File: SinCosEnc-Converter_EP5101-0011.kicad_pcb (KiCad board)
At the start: 2 copper layers, 88 x 49.3 mm, 4 parts, among them U1 iC-NV, X1 Conn_02x06_Top_Bottom, X2 D-SUB-DR-15PCG-AB

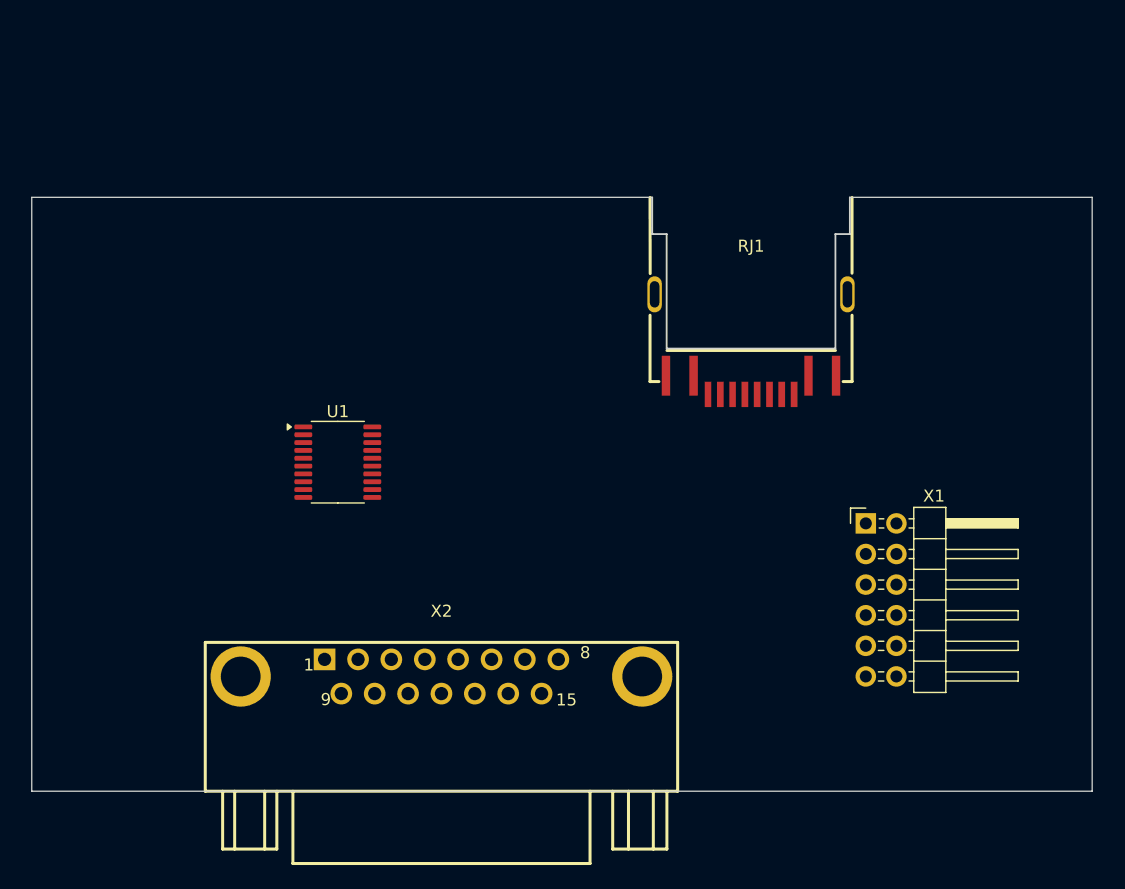
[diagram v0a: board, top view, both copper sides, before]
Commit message: schematic finished ~90%, layout: just outline done added mounting concept pictures
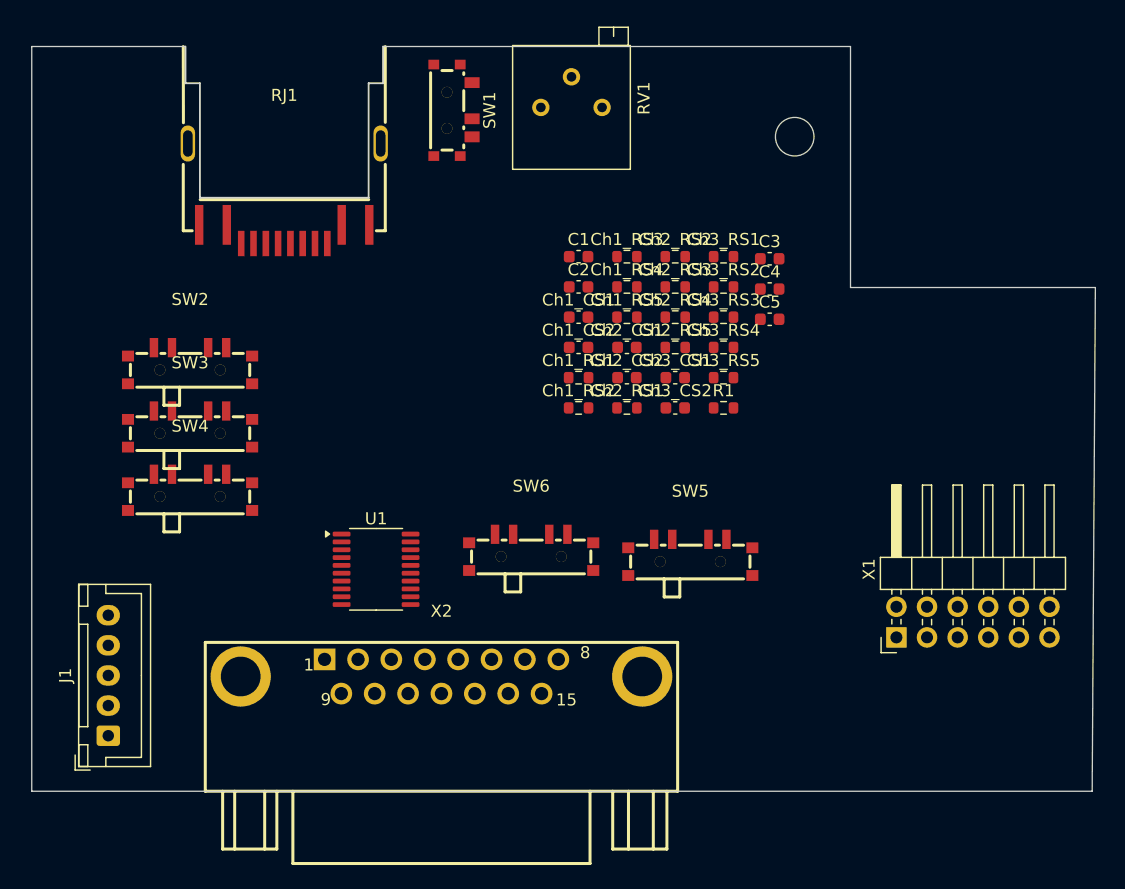
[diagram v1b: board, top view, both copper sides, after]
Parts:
- added C1: 100n, Capacitor_SMD:C_0603_1608Metric, F.Cu at (114.2, 71.1)
- added C2: 100n, Capacitor_SMD:C_0603_1608Metric, F.Cu at (114.2, 73.6)
- added C3: 4u7, Capacitor_SMD:C_0603_1608Metric, F.Cu at (130.1, 71.2)
- added C4: 100n, Capacitor_SMD:C_0603_1608Metric, F.Cu at (130.1, 73.7)
- added C5: 100n, Capacitor_SMD:C_0603_1608Metric, F.Cu at (130.1, 76.2)
- added Ch1_CS1: 220p, Capacitor_SMD:C_0603_1608Metric, F.Cu at (114.2, 76.1)
- added Ch1_CS2: 47n, Capacitor_SMD:C_0603_1608Metric, F.Cu at (114.2, 78.6)
- added Ch1_RS1: 120, Resistor_SMD:R_0603_1608Metric, F.Cu at (114.2, 81.1)
- added Ch1_RS2: 5k, Resistor_SMD:R_0603_1608Metric, F.Cu at (114.2, 83.6)
- added Ch1_RS3: 5k, Resistor_SMD:R_0603_1608Metric, F.Cu at (118.2, 71.1)
- added Ch1_RS4: 1k, Resistor_SMD:R_0603_1608Metric, F.Cu at (118.2, 73.6)
- added Ch1_RS5: 1k, Resistor_SMD:R_0603_1608Metric, F.Cu at (118.2, 76.1)
- added Ch2_CS1: 220p, Capacitor_SMD:C_0603_1608Metric, F.Cu at (118.2, 78.6)
- added Ch2_CS2: 47n, Capacitor_SMD:C_0603_1608Metric, F.Cu at (118.2, 81.1)
- added Ch2_RS1: 120, Resistor_SMD:R_0603_1608Metric, F.Cu at (118.2, 83.6)
- added Ch2_RS2: 5k, Resistor_SMD:R_0603_1608Metric, F.Cu at (122.2, 71.1)
- added Ch2_RS3: 5k, Resistor_SMD:R_0603_1608Metric, F.Cu at (122.2, 73.6)
- added Ch2_RS4: 1k, Resistor_SMD:R_0603_1608Metric, F.Cu at (122.2, 76.1)
- added Ch2_RS5: 1k, Resistor_SMD:R_0603_1608Metric, F.Cu at (122.2, 78.6)
- added Ch3_CS1: 220p, Capacitor_SMD:C_0603_1608Metric, F.Cu at (122.2, 81.1)
- added Ch3_CS2: 47n, Capacitor_SMD:C_0603_1608Metric, F.Cu at (122.2, 83.6)
- added Ch3_RS1: 120, Resistor_SMD:R_0603_1608Metric, F.Cu at (126.2, 71.1)
- added Ch3_RS2: 5k, Resistor_SMD:R_0603_1608Metric, F.Cu at (126.2, 73.6)
- added Ch3_RS3: 5k, Resistor_SMD:R_0603_1608Metric, F.Cu at (126.2, 76.1)
- added Ch3_RS4: 1k, Resistor_SMD:R_0603_1608Metric, F.Cu at (126.2, 78.6)
- added Ch3_RS5: 1k, Resistor_SMD:R_0603_1608Metric, F.Cu at (126.2, 81.1)
- added J1: Conn_01x05_Pin, Connector_JST:JST_XH_B5B-XH-A_1x05_P2.50mm_Vertical, F.Cu at (75.2, 110.8)
- added MH1: MountingHole_3.2mm_M3_ISO14580, MountingHole:MountingHole_3.2mm_M3_ISO14580, F.Cu at (132.1, 61.1)
- added R1: 330, Resistor_SMD:R_0603_1608Metric, F.Cu at (126.2, 83.6)
- added RV1: 500k, Potentiometer_THT:Potentiometer_Bourns_3296P_Horizontal, F.Cu at (116.1, 58.7)
- added SW1: SS-3292S-L2-W, CostumLibrary:SW-SMD_XKB_SS-3292S-L2-W, F.Cu at (103.8, 58.9)
- added SW2: SW_SG1, easyeda2kicad:SW-SMD_MSK13C02-BB, F.Cu at (82.0, 80.1)
- added SW3: SW_SG0, easyeda2kicad:SW-SMD_MSK13C02-BB, F.Cu at (82.0, 85.4)
- added SW4: SW_ROT, easyeda2kicad:SW-SMD_MSK13C02-BB, F.Cu at (82.0, 90.6)
- added SW5: SW_SF1, easyeda2kicad:SW-SMD_MSK13C02-BB, F.Cu at (123.5, 96.0)
- added SW6: SW_SF0, easyeda2kicad:SW-SMD_MSK13C02-BB, F.Cu at (110.3, 95.6)
- moved RJ1 40.7 mm to (89.8, 65.8)
- moved X1 9.80 mm to (140.6, 102.7), turned to 90 degrees
- moved U1 9.44 mm to (97.4, 97.0)
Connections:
- RJ1 pad 1: unconnected-(RJ1-Pad1) -> Sensor-V_in-1+
- RJ1 pad 10: unconnected-(RJ1-G+-Pad10) -> Net-(RJ1-G+)
- RJ1 pad 13: unconnected-(RJ1-SHELL-Pad13) -> CON_~{A}
- RJ1 pad 14: unconnected-(RJ1-SHELL-Pad14) -> CON_~{A}
- RJ1 pad 2: unconnected-(RJ1-Pad2) -> Sensor-V_in-1-
- RJ1 pad 3: unconnected-(RJ1-Pad3) -> CON_VCC
- RJ1 pad 4: unconnected-(RJ1-Pad4) -> CON_~{A}
- RJ1 pad 5: unconnected-(RJ1-Pad5) -> Sensor-V_in-2+
- RJ1 pad 6: unconnected-(RJ1-Pad6) -> Sensor-V_in-2-
- RJ1 pad 7: unconnected-(RJ1-Pad7) -> Sensor-V_in-0+
- RJ1 pad 8: unconnected-(RJ1-Pad8) -> Sensor-V_in-0-
- RJ1 pad 9: unconnected-(RJ1-G--Pad9) -> CON_~{A}
- U1 pad 1: unconnected-(U1-PCOS-Pad1) -> iC-V_in-2+
- U1 pad 10: unconnected-(U1-Z-Pad10) -> CON_C
- U1 pad 11: unconnected-(U1-B-Pad11) -> CON_B
- U1 pad 12: unconnected-(U1-A-Pad12) -> CON_A
- U1 pad 13: unconnected-(U1-VDD-Pad13) -> CON_VCC
- U1 pad 14: unconnected-(U1-RCLK-Pad14) -> Net-(SW1-B)
- U1 pad 15: unconnected-(U1-VCC-Pad15) -> CON_VCC
- U1 pad 16: unconnected-(U1-GNDA-Pad16) -> CON_~{A}
- U1 pad 17: unconnected-(U1-PZERO-Pad17) -> iC-V_in-0+
- U1 pad 18: unconnected-(U1-NZERO-Pad18) -> iC-V_in-0-
- U1 pad 19: unconnected-(U1-PSIN-Pad19) -> iC-V_in-1+
- U1 pad 2: unconnected-(U1-NCOS-Pad2) -> iC-V_in-2-
- U1 pad 20: unconnected-(U1-NSIN-Pad20) -> iC-V_in-1-
- U1 pad 3: unconnected-(U1-SG1-Pad3) -> iC-SG1
- U1 pad 4: unconnected-(U1-SG0-Pad4) -> iC-SG0
- U1 pad 5: unconnected-(U1-VREF-Pad5) -> iC-VREF
- U1 pad 6: unconnected-(U1-ROT-Pad6) -> iC-ROT
- U1 pad 7: unconnected-(U1-SF1-Pad7) -> iC-SF1
- U1 pad 8: unconnected-(U1-SF0-Pad8) -> iC-SF0
- U1 pad 9: unconnected-(U1-GND-Pad9) -> CON_~{A}
- X2 pad 1: unconnected-(X2-Pad1) -> CON_A
- X2 pad 10: unconnected-(X2-Pad10) -> CON_~{A}
- X2 pad 11: unconnected-(X2-Pad11) -> CON_~{A}
- X2 pad 12: unconnected-(X2-Pad12) -> CON_VCC
- X2 pad 13: unconnected-(X2-Pad13) -> CON_~{ERR}
- X2 pad 14: unconnected-(X2-Pad14) -> CON_~{A}
- X2 pad 15: unconnected-(X2-Pad15) -> CON_Gate
- X2 pad 16: unconnected-(X2-MH2-Pad16) -> CON_~{A}
- X2 pad 17: unconnected-(X2-MH1-Pad17) -> CON_~{A}
- X2 pad 2: unconnected-(X2-Pad2) -> CON_~{A}
- X2 pad 3: unconnected-(X2-Pad3) -> CON_B
- X2 pad 4: unconnected-(X2-Pad4) -> CON_VCC
- X2 pad 7: unconnected-(X2-Pad7) -> CON_C
- X2 pad 8: unconnected-(X2-Pad8) -> CON_Latch
- X2 pad 9: unconnected-(X2-Pad9) -> CON_~{A}
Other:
- board size 88 x 49.3 mm -> 88.3 x 61.8 mm

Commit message: minor progress
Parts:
- removed MH1: MountingHole_3.2mm_M3_ISO14580, MountingHole:MountingHole_3.2mm_M3_ISO14580
- removed X1: Conn_02x06_Top_Bottom, Connector_PinHeader_2.54mm:PinHeader_2x06_P2.54mm_Horizontal
- added J2: Conn_02x05_Top_Bottom, Connector_PinHeader_2.54mm:PinHeader_2x05_P2.54mm_Horizontal, F.Cu at (132.0, 100.3)
- Ch1_RS1, Ch2_RS1, Ch3_RS1: value 120 -> 5k
- Ch1_RS3, Ch2_RS3, Ch3_RS3: value 5k -> 1k
- Ch1_RS5, Ch2_RS5, Ch3_RS5: value 1k -> 120
- SW1: value SS-3292S-L2-W -> SW_RCLK
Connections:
- net CON_~{A} renamed GND
- Ch1_RS1 pad 1: Sensor-V_in-1+ -> iC-VREF
- Ch1_RS1 pad 2: Sensor-V_in-1- -> Sensor-V_in-1+
- Ch1_RS2 pad 1: iC-VREF -> Sensor-V_in-1-
- Ch1_RS2 pad 2: Sensor-V_in-1+ -> iC-VREF
- Ch1_RS3 pad 1: Sensor-V_in-1- -> Sensor-V_in-1+
- Ch1_RS3 pad 2: iC-VREF -> iC-V_in-1+
- Ch1_RS4 pad 1: Sensor-V_in-1+ -> Sensor-V_in-1-
- Ch1_RS4 pad 2: iC-V_in-1+ -> iC-V_in-1-
- Ch1_RS5 pad 1: Sensor-V_in-1- -> Sensor-V_in-1+
- Ch1_RS5 pad 2: iC-V_in-1- -> Sensor-V_in-1-
- Ch2_RS1 pad 1: Sensor-V_in-2+ -> iC-VREF
- Ch2_RS1 pad 2: Sensor-V_in-2- -> Sensor-V_in-2+
- Ch2_RS2 pad 1: iC-VREF -> Sensor-V_in-2-
- Ch2_RS2 pad 2: Sensor-V_in-2+ -> iC-VREF
- Ch2_RS3 pad 1: Sensor-V_in-2- -> Sensor-V_in-2+
- Ch2_RS3 pad 2: iC-VREF -> iC-V_in-2+
- Ch2_RS4 pad 1: Sensor-V_in-2+ -> Sensor-V_in-2-
- Ch2_RS4 pad 2: iC-V_in-2+ -> iC-V_in-2-
- Ch2_RS5 pad 1: Sensor-V_in-2- -> Sensor-V_in-2+
- Ch2_RS5 pad 2: iC-V_in-2- -> Sensor-V_in-2-
- Ch3_RS1 pad 1: Sensor-V_in-0+ -> iC-VREF
- Ch3_RS1 pad 2: Sensor-V_in-0- -> Sensor-V_in-0+
- Ch3_RS2 pad 1: iC-VREF -> Sensor-V_in-0-
- Ch3_RS2 pad 2: Sensor-V_in-0+ -> iC-VREF
- Ch3_RS3 pad 1: Sensor-V_in-0- -> Sensor-V_in-0+
- Ch3_RS3 pad 2: iC-VREF -> iC-V_in-0+
- Ch3_RS4 pad 1: Sensor-V_in-0+ -> Sensor-V_in-0-
- Ch3_RS4 pad 2: iC-V_in-0+ -> iC-V_in-0-
- Ch3_RS5 pad 1: Sensor-V_in-0- -> Sensor-V_in-0+
- Ch3_RS5 pad 2: iC-V_in-0- -> Sensor-V_in-0-

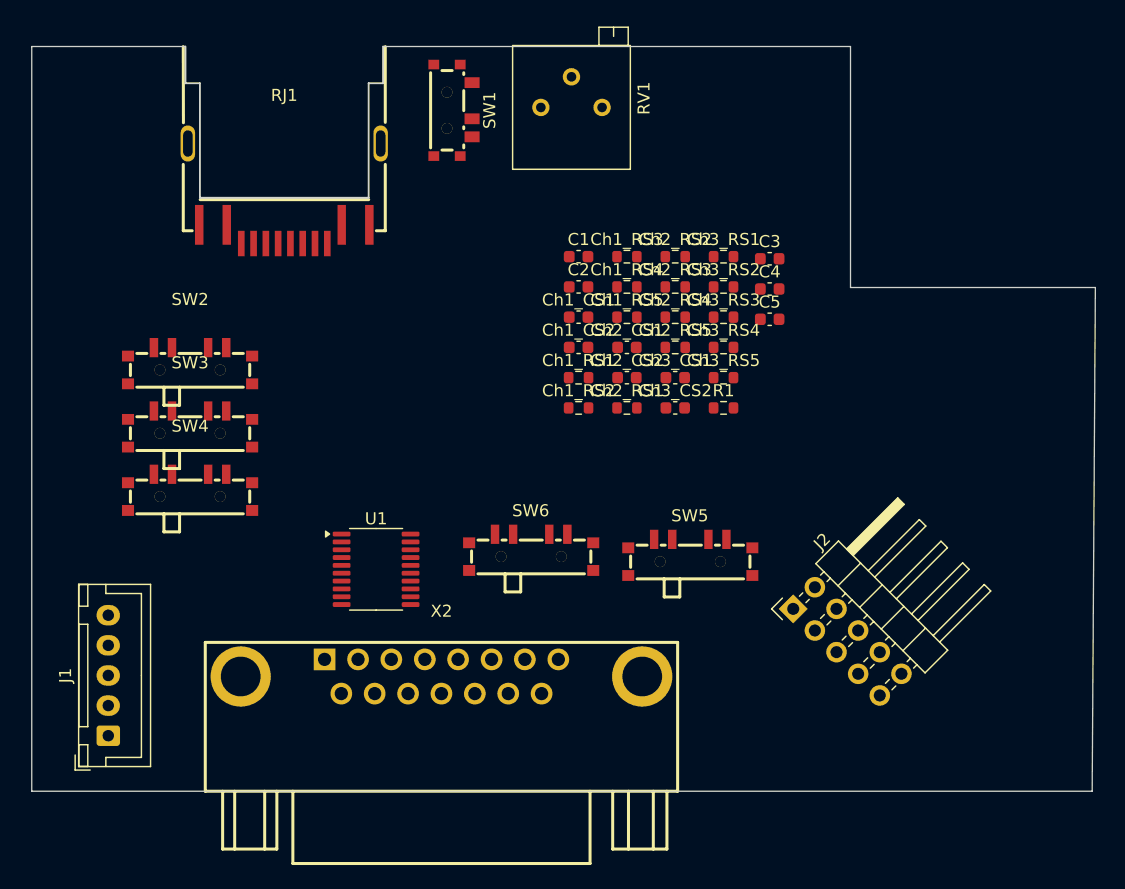
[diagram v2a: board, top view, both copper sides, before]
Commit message: further ESD protection, PCB layout started
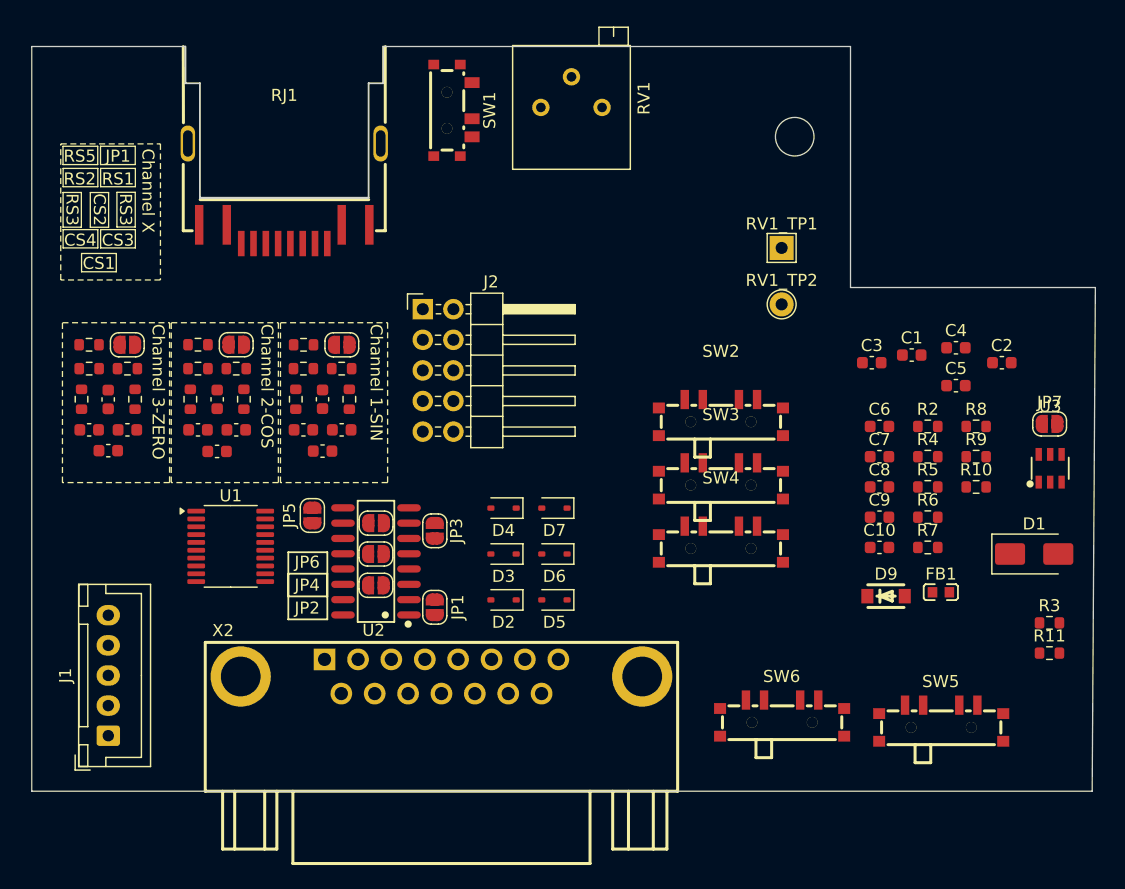
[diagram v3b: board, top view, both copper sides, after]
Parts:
- removed R1: 330, Resistor_SMD:R_0603_1608Metric
- added C10: 0.1u, Capacitor_SMD:C_0603_1608Metric, F.Cu at (139.2, 95.2)
- added C6: 100n, Capacitor_SMD:C_0603_1608Metric, F.Cu at (139.2, 85.1)
- added C7: 100n, Capacitor_SMD:C_0603_1608Metric, F.Cu at (139.2, 87.7)
- added C8: 1u, Capacitor_SMD:C_0603_1608Metric, F.Cu at (139.2, 90.2)
- added C9: 10u, Capacitor_SMD:C_0603_1608Metric, F.Cu at (139.2, 92.7)
- added Ch1_CS3: 470p, Capacitor_SMD:C_0603_1608Metric, F.Cu at (94.5, 85.4)
- added Ch1_CS4: 470p, Capacitor_SMD:C_0603_1608Metric, F.Cu at (91.4, 85.4)
- added Ch1_JP1: activate 1V_{PP}, Jumper:SolderJumper-2_P1.3mm_Open_RoundedPad1.0x1.5mm, F.Cu at (94.5, 78.4)
- added Ch2_CS3: 470p, Capacitor_SMD:C_0603_1608Metric, F.Cu at (76.8, 85.4)
- added Ch2_CS4: 470p, Capacitor_SMD:C_0603_1608Metric, F.Cu at (73.6, 85.4)
- added Ch2_JP1: activate 1V_{PP}, Jumper:SolderJumper-2_P1.3mm_Open_RoundedPad1.0x1.5mm, F.Cu at (76.7, 78.4)
- added Ch3_CS3: 470p, Capacitor_SMD:C_0603_1608Metric, F.Cu at (85.8, 85.4)
- added Ch3_CS4: 470p, Capacitor_SMD:C_0603_1608Metric, F.Cu at (82.6, 85.4)
- added Ch3_JP1: activate 1V_{PP}, Jumper:SolderJumper-2_P1.3mm_Open_RoundedPad1.0x1.5mm, F.Cu at (85.8, 78.4)
- added D1: 1N4007, Diode_SMD:D_SMA, F.Cu at (152.0, 95.7)
- added D2: SD15, Diode_SMD:D_SOD-323, F.Cu at (108.0, 99.5)
- added D3: SD15, Diode_SMD:D_SOD-323, F.Cu at (108.0, 95.7)
- added D4: SD15, Diode_SMD:D_SOD-323, F.Cu at (108.0, 91.9)
- added D5: SD15, Diode_SMD:D_SOD-323, F.Cu at (112.2, 99.5)
- added D6: SD15, Diode_SMD:D_SOD-323, F.Cu at (112.2, 95.7)
- added D7: SD15, Diode_SMD:D_SOD-323, F.Cu at (112.2, 91.9)
- added D9: SMF5.0A, easyeda2kicad:SOD-123F_L2.8-W1.8-LS3.7-RD, F.Cu at (139.7, 99.2)
- added FB1: 100R@100MHz, easyeda2kicad:L0603, F.Cu at (144.3, 98.9)
- added JP1: SingleEnded_A, Jumper:SolderJumper-2_P1.3mm_Open_RoundedPad1.0x1.5mm, F.Cu at (102.3, 100.2)
- added JP2: CON_~{A} to GND, Jumper:SolderJumper-2_P1.3mm_Open_RoundedPad1.0x1.5mm, F.Cu at (97.4, 98.3)
- added JP3: SingleEnded_B, Jumper:SolderJumper-2_P1.3mm_Open_RoundedPad1.0x1.5mm, F.Cu at (102.3, 93.8)
- added JP4: CON_~{B} to GND, Jumper:SolderJumper-2_P1.3mm_Open_RoundedPad1.0x1.5mm, F.Cu at (97.4, 95.7)
- added JP5: SingleEnded_C, Jumper:SolderJumper-2_P1.3mm_Open_RoundedPad1.0x1.5mm, F.Cu at (92.1, 92.5)
- added JP6: CON_~{C} to GND, Jumper:SolderJumper-2_P1.3mm_Open_RoundedPad1.0x1.5mm, F.Cu at (97.4, 93.2)
- added JP7: noILIM, Jumper:SolderJumper-2_P1.3mm_Open_RoundedPad1.0x1.5mm, F.Cu at (153.3, 84.9)
- added MH1: MountingHole_3.2mm_M3_ISO14580, MountingHole:MountingHole_3.2mm_M3_ISO14580, F.Cu at (132.1, 61.1)
- added R10: 0, Resistor_SMD:R_0603_1608Metric, F.Cu at (147.2, 90.2)
- added R11: 470, Resistor_SMD:R_0603_1608Metric, F.Cu at (153.3, 104.0)
- added R2: 180k, Resistor_SMD:R_0603_1608Metric, F.Cu at (143.2, 85.1)
- added R3: 470, Resistor_SMD:R_0603_1608Metric, F.Cu at (153.3, 101.4)
- added R4: 0, Resistor_SMD:R_0603_1608Metric, F.Cu at (143.2, 87.7)
- added R5: 0, Resistor_SMD:R_0603_1608Metric, F.Cu at (143.2, 90.2)
- added R6: 0, Resistor_SMD:R_0603_1608Metric, F.Cu at (143.2, 92.7)
- added R7: 0, Resistor_SMD:R_0603_1608Metric, F.Cu at (143.2, 95.2)
- added R8: 0, Resistor_SMD:R_0603_1608Metric, F.Cu at (147.2, 85.1)
- added R9: 0, Resistor_SMD:R_0603_1608Metric, F.Cu at (147.2, 87.7)
- added RV1_TP1: TestPoint_RV1, TestPoint:TestPoint_THTPad_2.0x2.0mm_Drill1.0mm, F.Cu at (131.0, 70.3)
- added RV1_TP2: TestPoint_RV1, TestPoint:TestPoint_THTPad_D2.0mm_Drill1.0mm, F.Cu at (131.0, 75.0)
- added U2: AM26LS31CDR, easyeda2kicad:SOIC-16_L9.9-W3.9-P1.27-LS6.0-BL, F.Cu at (97.4, 96.3)
- added U3: AP22652AW6-7, easyeda2kicad:SOT-23-6_L2.9-W1.6-P0.95-LS2.8-BL, F.Cu at (153.3, 88.6)
- Ch1_RS1, Ch1_RS2, Ch2_RS1, Ch2_RS2, Ch3_RS1, Ch3_RS2: value 5k -> 50k
- moved Ch2_RS4 49.7 mm to (72.9, 82.9), turned to -90 degrees
- moved Ch2_RS2 49.5 mm to (73.6, 80.3)
- moved Ch2_RS5 48.6 mm to (73.6, 78.4), turned to 180 degrees
- moved Ch2_RS3 45.8 mm to (77.4, 82.9), turned to -90 degrees
- moved Ch3_RS4 44.5 mm to (82.0, 82.9), turned to -90 degrees
- moved SW2 44.3 mm to (126.0, 84.4)
- moved SW3 44.3 mm to (126.0, 89.7)
- moved SW4 44.3 mm to (126.0, 94.9)
- moved Ch3_RS2 44.1 mm to (82.6, 80.3)
- moved Ch2_CS1 43.9 mm to (75.2, 87.2), turned to 180 degrees
- moved Ch3_RS5 43.7 mm to (82.6, 78.4), turned to 180 degrees
- moved Ch2_CS2 43.1 mm to (75.2, 82.9), turned to -90 degrees
- moved Ch2_RS1 41.6 mm to (76.8, 80.3)
- moved Ch3_RS1 41.5 mm to (85.8, 80.3)
- moved Ch3_RS3 40.4 mm to (86.4, 82.9), turned to -90 degrees
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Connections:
- net Sensor-V_in-0- renamed Sensor_IN_ZERO-
- net Sensor-V_in-2- renamed Sensor_IN_COS-
- net iC-V_in-0+ renamed iC-ZERO+
- net iC-V_in-0- renamed iC-ZERO-
- net iC-V_in-2+ renamed iC-COS+
- net iC-V_in-2- renamed iC-COS-
- C1 pad 2: CON_VCC -> +5V
- C2 pad 2: CON_VCC -> +5V
- C3 pad 2: CON_VCC -> +5V_Sensor
- Ch1_CS1 pad 1: iC-V_in-1+ -> iC-SIN+
- Ch1_CS1 pad 2: iC-V_in-1- -> iC-SIN-
- Ch1_RS1 pad 2: Sensor-V_in-1+ -> Sensor_IN_SIN+
- Ch1_RS2 pad 1: Sensor-V_in-1- -> Sensor_IN_SIN-
- Ch1_RS3 pad 1: Sensor-V_in-1+ -> iC-SIN+
- Ch1_RS3 pad 2: iC-V_in-1+ -> Sensor_IN_SIN+
- Ch1_RS4 pad 1: Sensor-V_in-1- -> iC-SIN-
- Ch1_RS4 pad 2: iC-V_in-1- -> Sensor_IN_SIN-
- Ch1_RS5 pad 1: Sensor-V_in-1+ -> Net-(Ch1_JP1-A)
- Ch1_RS5 pad 2: Sensor-V_in-1- -> Sensor_IN_SIN-
- Ch2_RS1 pad 2: Sensor-V_in-2+ -> Sensor_IN_COS+
- Ch2_RS3 pad 1: Sensor-V_in-2+ -> Sensor_IN_COS+
- Ch2_RS5 pad 1: Sensor-V_in-2+ -> Net-(Ch2_JP1-A)
- Ch3_RS1 pad 2: Sensor-V_in-0+ -> Sensor_IN_ZERO+
- Ch3_RS3 pad 1: Sensor-V_in-0+ -> Sensor_IN_ZERO+
- Ch3_RS5 pad 1: Sensor-V_in-0+ -> Net-(Ch3_JP1-A)
- J2 pad 1: Sensor-V_in-1+ -> Sensor_IN_SIN+
- J2 pad 2: Sensor-V_in-1- -> Sensor_IN_SIN-
- J2 pad 3: CON_VCC -> +5V_Sensor
- J2 pad 5: Sensor-V_in-2+ -> Sensor_IN_COS+
- J2 pad 7: Sensor-V_in-0+ -> Sensor_IN_ZERO+
- RJ1 pad 1: Sensor-V_in-1+ -> Sensor_IN_SIN+
- RJ1 pad 11: unconnected-(RJ1-Y--Pad11) -> CON_~{ERR}
- RJ1 pad 12: unconnected-(RJ1-Y+-Pad12) -> Net-(RJ1-Y+)
- RJ1 pad 2: Sensor-V_in-1- -> Sensor_IN_SIN-
- RJ1 pad 3: CON_VCC -> +5V_Sensor
- RJ1 pad 5: Sensor-V_in-2+ -> Sensor_IN_COS+
- RJ1 pad 7: Sensor-V_in-0+ -> Sensor_IN_ZERO+
- SW1 pad 3: CON_VCC -> +5V
- SW1 pad Sh: unconnected-(SW1-PadSh) -> GND
- SW2 pad 2: CON_VCC -> +5V
- SW3 pad 2: CON_VCC -> +5V
- SW4 pad 2: CON_VCC -> +5V
- SW5 pad 2: CON_VCC -> +5V
- SW6 pad 2: CON_VCC -> +5V
- U1 pad 10: CON_C -> TTL_Sig_C
- U1 pad 11: CON_B -> TTL_Sig_B
- U1 pad 12: CON_A -> TTL_Sig_A
- U1 pad 13: CON_VCC -> +5V
- U1 pad 15: CON_VCC -> +5V
- U1 pad 19: iC-V_in-1+ -> iC-SIN+
- U1 pad 20: iC-V_in-1- -> iC-SIN-
- X2 pad 1: CON_A -> DifSig_A+
- X2 pad 11: GND -> DifSig_B-
- X2 pad 14: GND -> DifSig_C+
- X2 pad 3: CON_B -> DifSig_B+
- X2 pad 7: CON_C -> DifSig_C-
- X2 pad 9: GND -> DifSig_A-
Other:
- board text added: "CS1"
- board text added: "CS2"
- board text added: "CS3"
- board text added: "CS4"
- board text added: "Channel 1-SIN"
- board text added: "Channel 2-COS"
- board text added: "Channel 3-ZERO"
- board text added: "Channel X"
- board text added: "JP1"
- board text added: "RS1"
- board text added: "RS2"
- board text added: "RS3"
- board text added: "RS5"
